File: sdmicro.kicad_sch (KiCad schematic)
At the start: 0 parts

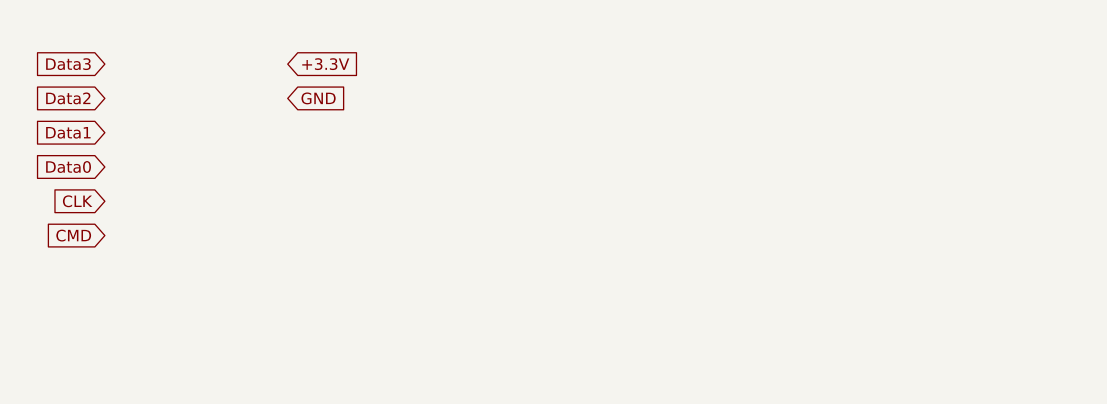
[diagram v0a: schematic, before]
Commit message: Initial component symbol placement
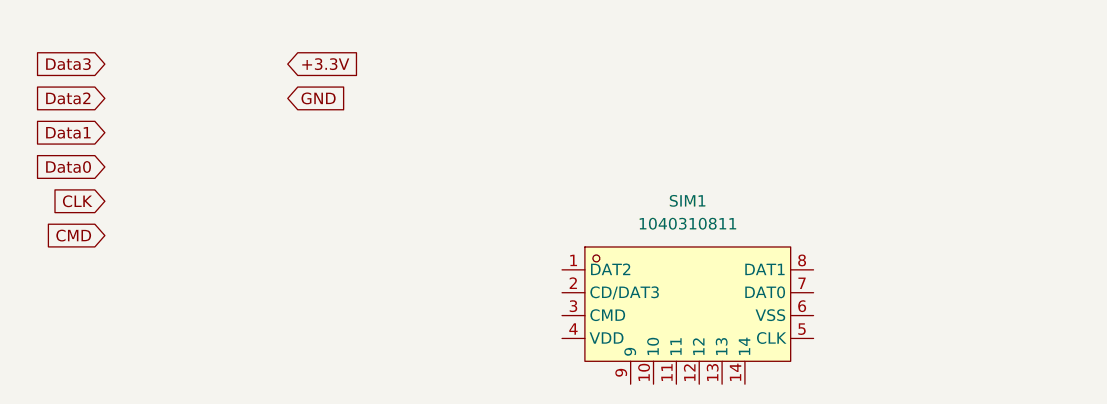
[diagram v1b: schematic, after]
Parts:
- added SIM1: 1040310811, Library:SIM-SMD_8P-1040310811, symbol Library:1040310811
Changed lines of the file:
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@@
+		)
+	)
+	(symbol
+		(lib_id "Library:1040310811")
+		(at 171.45 90.17 0)
+		(unit 1)
+		(exclude_from_sim no)
+		(in_bom yes)
+		(on_board yes)
+		(dnp no)
+		(fields_autoplaced yes)
+		(property "Reference" "SIM1"
+			(at 171.45 77.47 0)
+			(effects
+				(font
+					(size 1.27 1.27)
+				)
+			)
+		)
+		(property "Value" "1040310811"
+			(at 171.45 80.01 0)
+			(effects
+				(font
+					(size 1.27 1.27)
+				)
+			)
+		)
+		(property "Footprint" "Library:SIM-SMD_8P-1040310811"
+			(at 171.45 105.41 0)
+			(effects
+				(font
+					(size 1.27 1.27)
+				)
+				(hide yes)
+			)
+		)
+		(property "Datasheet" "https://www.lcsc.com/datasheet/C585350.pdf"
+			(at 171.45 107.95 0)
+			(effects
+				(font
+					(size 1.27 1.27)
+				)
+				(hide yes)
+			)
+		)
+		(property "Description" ""
+			(at 171.45 90.17 0)
+			(effects
+				(font
+					(size 1.27 1.27)
+				)
+				(hide yes)
+			)
+		)
+		(property "Manufacturer" "MOLEX"
+			(at 171.45 110.49 0)
+			(effects
+				(font
+					(size 1.27 1.27)
+				)
+				(hide yes)
+			)
+		)
+		(property "MPN" "1040310811"
+			(at 171.45 113.03 0)
+			(effects
+				(font
+					(size 1.27 1.27)
+				)
+				(hide yes)
+			)
+		)
+		(property "LCSC Part" "C585350"
+			(at 171.45 115.57 0)
+			(effects
+				(font
+					(size 1.27 1.27)
+				)
+				(hide yes)
+			)
+		)
+		(pin "9"
+		)
+		(pin "12"
+		)
+		(pin "10"
+		)
+		(pin "7"
+		)
+		(pin "5"
+		)
+		(pin "2"
+		)
+		(pin "13"
+		)
+		(pin "3"
+		)
+		(pin "14"
+		)
+		(pin "6"
+		)
+		(pin "4"
+		)
+		(pin "8"
+		)
+		(pin "1"
+		)
+		(pin "11"
+		)
+		(instances
+			(project ""
+				(path "/6af311bf-2fb1-446c-8c7e-7c930a463809/18e476ff-ff3f-4c6f-b30c-c422568368bf"
+					(reference "SIM1")
+					(unit 1)
+				)
+			)
 		)
 	)

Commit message: Barometer & ToF Hierarchical Schematic Updates
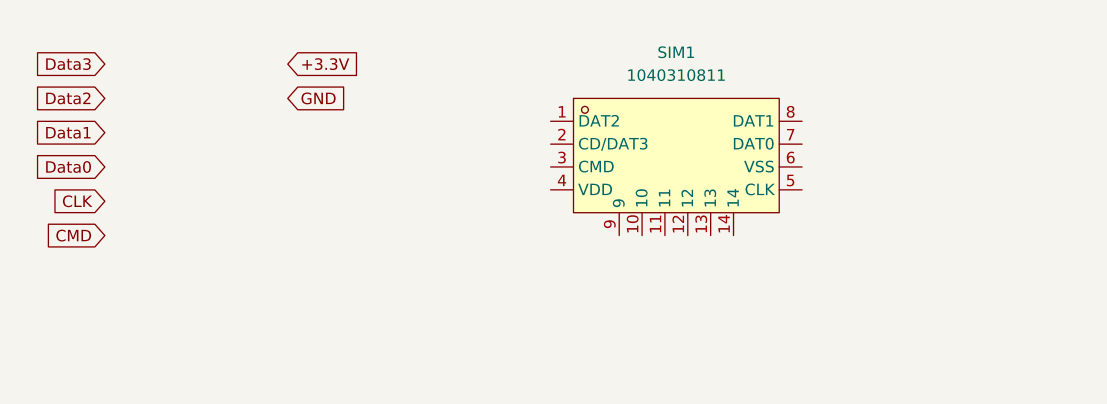
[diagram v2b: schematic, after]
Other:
- moved on the sheet: SIM1
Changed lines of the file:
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@@
 	(symbol
 		(lib_id "Library:1040310811")
-		(at 171.45 90.17 0)
+		(at 170.18 73.66 0)
 		(unit 1)
 		(exclude_from_sim no)
@@
 		(fields_autoplaced yes)
 		(property "Reference" "SIM1"
-			(at 171.45 77.47 0)
+			(at 170.18 60.96 0)
 			(effects
 				(font
@@
 		)
 		(property "Value" "1040310811"
-			(at 171.45 80.01 0)
+			(at 170.18 63.5 0)
 			(effects
 				(font
@@
 		)
 		(property "Footprint" "Library:SIM-SMD_8P-1040310811"
-			(at 171.45 105.41 0)
+			(at 170.18 88.9 0)
 			(effects
 				(font
@@
 		)
 		(property "Datasheet" "https://www.lcsc.com/datasheet/C585350.pdf"
-			(at 171.45 107.95 0)
+			(at 170.18 91.44 0)
 			(effects
 				(font
@@
 		)
 		(property "Description" ""
-			(at 171.45 90.17 0)
+			(at 170.18 73.66 0)
 			(effects
 				(font
@@
 		)
 		(property "Manufacturer" "MOLEX"
-			(at 171.45 110.49 0)
+			(at 170.18 93.98 0)
 			(effects
 				(font
@@
 		)
 		(property "MPN" "1040310811"
-			(at 171.45 113.03 0)
+			(at 170.18 96.52 0)
 			(effects
 				(font
@@
 		)
 		(property "LCSC Part" "C585350"
-			(at 171.45 115.57 0)
+			(at 170.18 99.06 0)
 			(effects
 				(font

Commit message: MCU implementation start Still needs component schematic checks & component integration with MCU
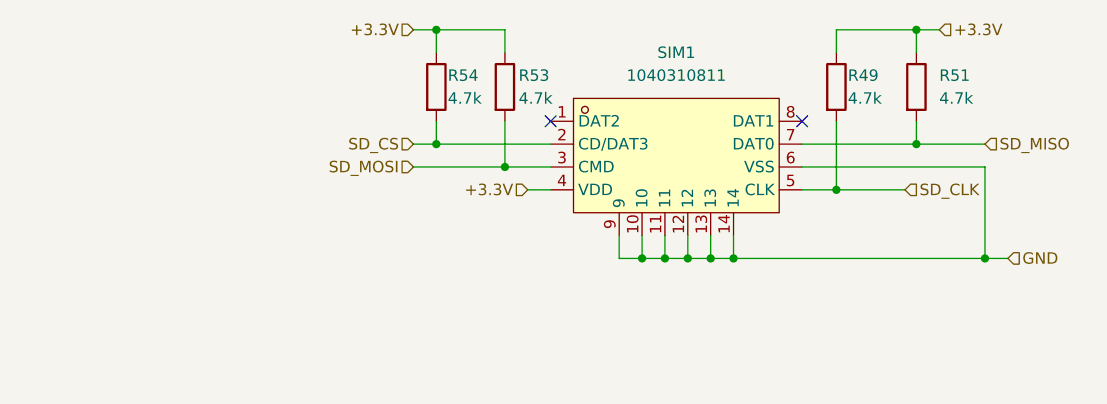
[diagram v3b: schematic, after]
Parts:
- added R49, R51, R53, R54: 4.7k, symbol Device:R
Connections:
- net +3.3V: now also SIM1.4 (VDD), R49.1, R51.1, R53.1, R54.1
- net GND: now also SIM1.10, SIM1.11, SIM1.12, SIM1.13, SIM1.14, SIM1.6 (VSS), SIM1.9
- net SD_CS: now reaches SIM1.2 (CD/DAT3)
- net SD_CS: now also R54.2
- net SD_MOSI: now reaches SIM1.3 (CMD)
- net SD_MOSI: now also R53.2
- net SD_CLK: now reaches SIM1.5 (CLK)
- net SD_CLK: now also R49.2
- net SD_MISO: now reaches SIM1.7 (DAT0)
- net SD_MISO: now also R51.2
- no-connect marks 0 -> 2

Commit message: MCU Integration & Sensor Ports
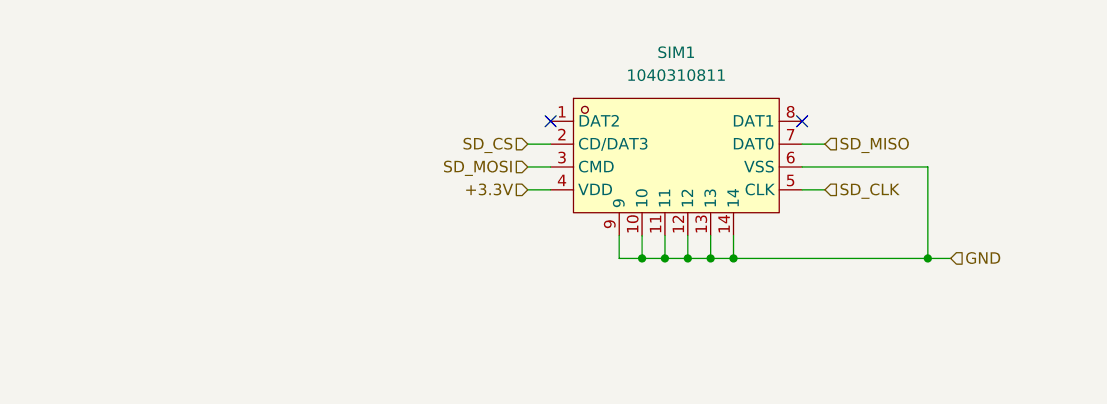
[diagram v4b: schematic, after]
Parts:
- removed R49, R51, R53, R54: 4.7k, symbol Device:R
